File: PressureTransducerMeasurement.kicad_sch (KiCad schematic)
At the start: 24 parts, among them J10 PT_6, J5 PT_1, J6 PT_4, J7 PT_2, J8 PT_5, J9 PT_3

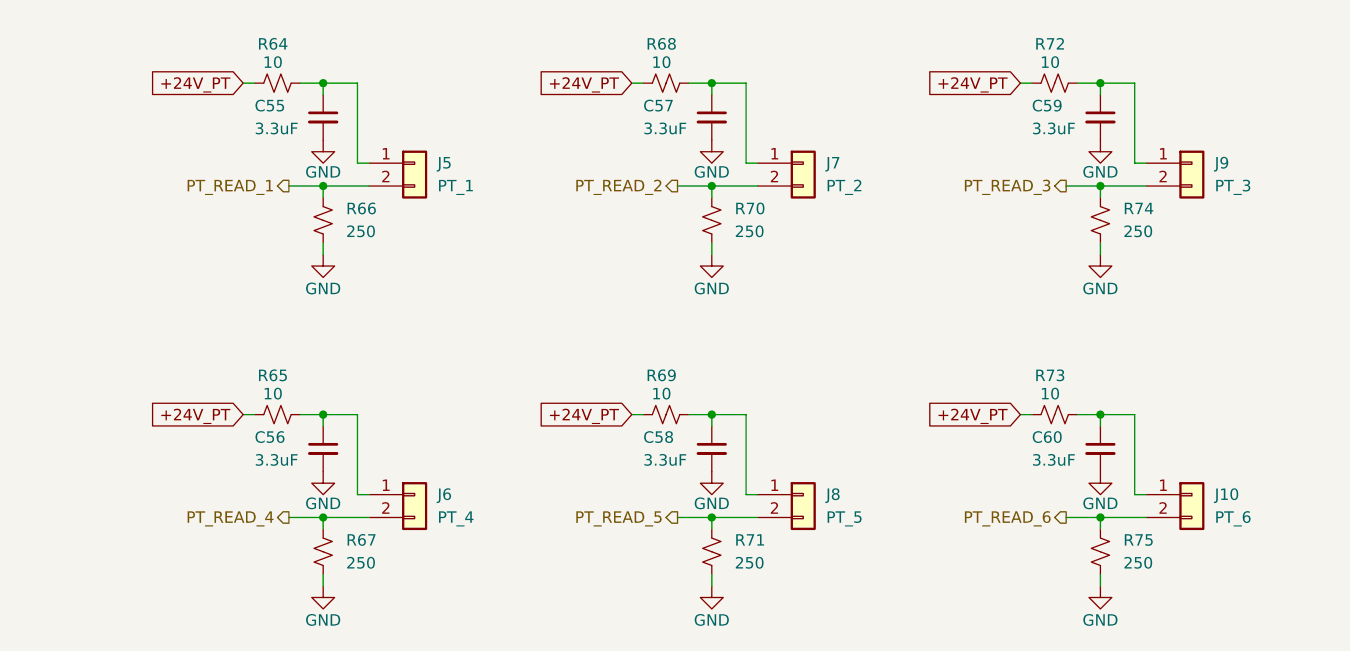
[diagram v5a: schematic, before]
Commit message: change connectors and more progress on pcb
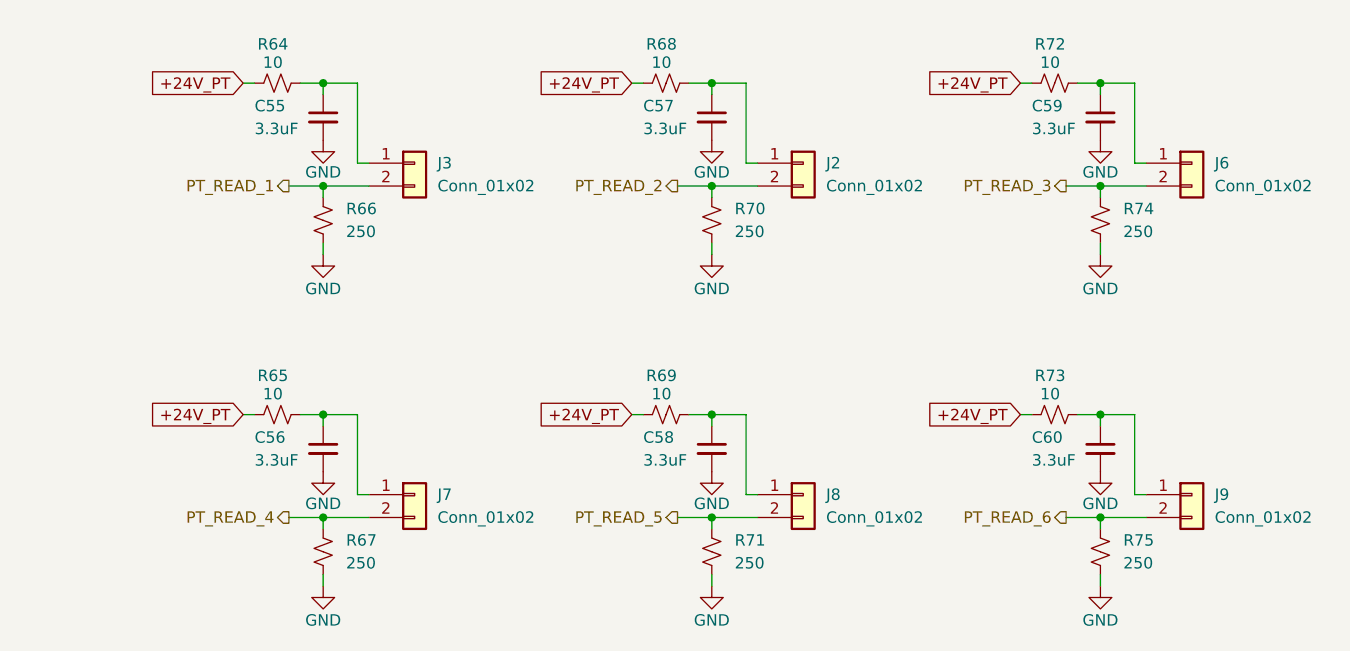
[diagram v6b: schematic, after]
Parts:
- removed J10: PT_6, Connector_JST:JST_XH_B2B-XH-A_1x02_P2.50mm_Vertical, symbol Connector_Generic:Conn_01x02
- removed J5: PT_1, Connector_JST:JST_XH_B2B-XH-A_1x02_P2.50mm_Vertical, symbol Connector_Generic:Conn_01x02
- added J2, J3: Conn_01x02, Connector_Molex:Molex_Micro-Fit_3.0_43650-0215_1x02_P3.00mm_Vertical, symbol Connector_Generic:Conn_01x02
- J6: value PT_4 -> Conn_01x02; footprint Connector_JST:JST_XH_B2B-XH-A_1x02_P2.50mm_Vertical -> Connector_Molex:Molex_Micro-Fit_3.0_43650-0215_1x02_P3.00mm_Vertical; LCSC C20079 -> (none); MPN XH-2A -> (none); now in the parts list
- J7: value PT_2 -> Conn_01x02; footprint Connector_JST:JST_XH_B2B-XH-A_1x02_P2.50mm_Vertical -> Connector_Molex:Molex_Micro-Fit_3.0_43650-0215_1x02_P3.00mm_Vertical; LCSC C20079 -> (none); MPN XH-2A -> (none); now in the parts list
- J8: value PT_5 -> Conn_01x02; footprint Connector_JST:JST_XH_B2B-XH-A_1x02_P2.50mm_Vertical -> Connector_Molex:Molex_Micro-Fit_3.0_43650-0215_1x02_P3.00mm_Vertical; LCSC C20079 -> (none); MPN XH-2A -> (none); now in the parts list
- J9: value PT_3 -> Conn_01x02; footprint Connector_JST:JST_XH_B2B-XH-A_1x02_P2.50mm_Vertical -> Connector_Molex:Molex_Micro-Fit_3.0_43650-0215_1x02_P3.00mm_Vertical; LCSC C20079 -> (none); MPN XH-2A -> (none); now in the parts list
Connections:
- net PT_READ_1: now also J3.2 (Pin_2)
- net PT_READ_2: now also J2.2 (Pin_2); no longer J7.2 (Pin_2)
- net PT_READ_3: now also J6.2 (Pin_2); no longer J9.2 (Pin_2)
- net PT_READ_4: now also J7.2 (Pin_2); no longer J6.2 (Pin_2)
- net PT_READ_6: now also J9.2 (Pin_2)
- net at C59.1, R72.2: now also J6.1 (Pin_1); no longer J9.1 (Pin_1)
- net at C56.1, R65.2: now also J7.1 (Pin_1); no longer J6.1 (Pin_1)
- net at C60.1, R73.2: now also J9.1 (Pin_1)
- net at C57.1, R68.2: now also J2.1 (Pin_1); no longer J7.1 (Pin_1)
- net at C55.1, R64.2: now also J3.1 (Pin_1)

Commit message: change clamping resistors on tc adcs for lower leakage current
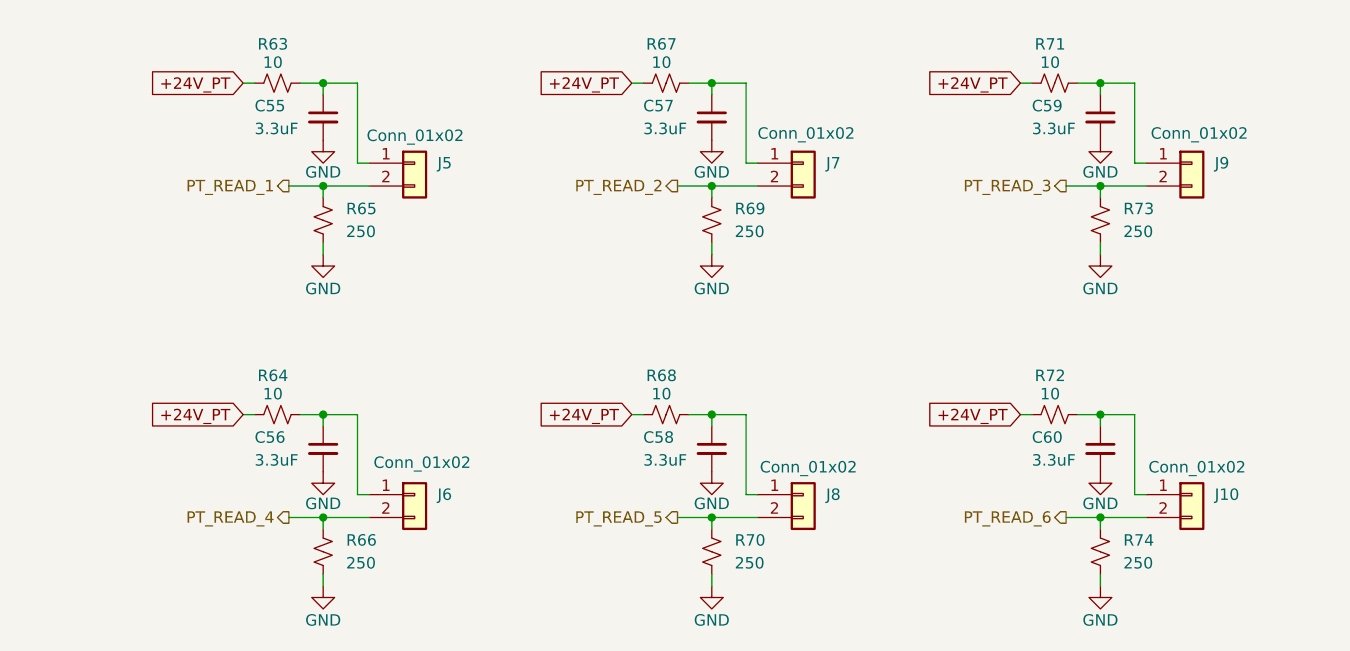
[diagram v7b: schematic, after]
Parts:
- renumbered J9 to J10, J3 to J5, J7 to J6, J2 to J7, J6 to J9, R64 to R63, R65 to R64, R66 to R65, R67 to R66, R68 to R67, R69 to R68, R70 to R69, R71 to R70, R72 to R71, R73 to R72, R74 to R73, R75 to R74

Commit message: Update version number in KiCad files
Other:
- title: Pressure Transducer Measurement -> PANDA
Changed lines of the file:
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@@
 	(paper "A4")
 	(title_block
-		(title "Pressure Transducer Measurement")
-		(rev "1.0.0")
+		(title "PANDA")
+		(date "2025-12-21")
+		(rev "3.0.0")
 		(company "Queen's Rocket Engineering Team")
 	)
@@
 		(polyline
 			(pts
+				(xy 87.63 62.23) (xy 128.27 62.23) (xy 128.27 93.98) (xy 87.63 93.98)
+			)
+			(stroke
+				(width 0)
+				(type dash)
+			)
+			(fill
+				(type none)
+			)
+		)
+	)
+	(rule_area
+		(polyline
+			(pts
+				(xy 173.99 62.23) (xy 214.63 62.23) (xy 214.63 93.98) (xy 173.99 93.98)
+			)
+			(stroke
+				(width 0)
+				(type dash)
+			)
+			(fill
+				(type none)
+			)
+		)
+	)
+	(rule_area
+		(polyline
+			(pts
+				(xy 87.63 99.06) (xy 128.27 99.06) (xy 128.27 130.81) (xy 87.63 130.81)
+			)
+			(stroke
+				(width 0)
+				(type dash)
+			)
+			(fill
+				(type none)
+			)
+		)
+	)
+	(rule_area
+		(polyline
+			(pts
 				(xy 173.99 99.06) (xy 214.63 99.06) (xy 214.63 130.81) (xy 173.99 130.81)
 			)
@@
 			)
 			(stroke
-				(width 0)
-				(type dash)
-			)
-			(fill
-				(type none)
-			)
-		)
-	)
-	(rule_area
-		(polyline
-			(pts
-				(xy 87.63 62.23) (xy 128.27 62.23) (xy 128.27 93.98) (xy 87.63 93.98)
-			)
-			(stroke
-				(width 0)
-				(type dash)
-			)
-			(fill
-				(type none)
-			)
-		)
-	)
-	(rule_area
-		(polyline
-			(pts
-				(xy 87.63 99.06) (xy 128.27 99.06) (xy 128.27 130.81) (xy 87.63 130.81)
-			)
-			(stroke
-				(width 0)
-				(type dash)
-			)
-			(fill
-				(type none)
-			)
-		)
-	)
-	(rule_area
-		(polyline
-			(pts
-				(xy 173.99 62.23) (xy 214.63 62.23) (xy 214.63 93.98) (xy 173.99 93.98)
-			)
-			(stroke
